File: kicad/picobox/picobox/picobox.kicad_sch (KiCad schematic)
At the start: 31 parts, among them J1 Conn_01x02, J2 Conn_01x03, J3 Conn_01x03, J4 Conn_01x03, J5 Conn_01x03, J6 Conn_01x03, J7 Conn_01x03, J8 Conn_01x03, J9 Conn_01x10, SW1 SW_SPDT, U1 MCP1703Ax-330xxDB

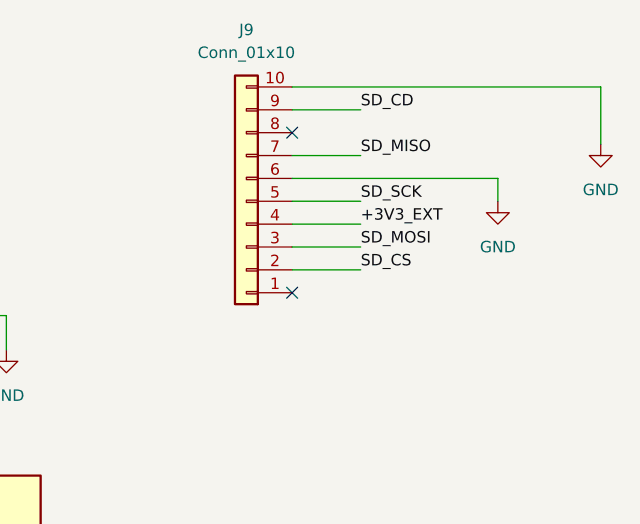
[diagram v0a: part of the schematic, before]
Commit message: feat: PicoBox PCB完成・部品発注完了
- PCBレイアウト・DRC完了（エラー0件）、JLCPCB発注済み（5枚 $4.64）
- J9ピンアサイン修正（SD_CD=PIN10, GND=PIN9）
- Gerberファイル追加（kicad/gerver.zip）
- KiCAD PCBレイアウト・回路図最終版を反映
- docs/pcb_spec.md: 全部品の購入先・品番確定、調達状況セクション追加
  - Mouser: MCP1703 / P6KE6.8CA-TB / SPTAF端子台 / Pico W / SD-15B-05
  - 秋月: 抵抗・コンデンサ・LED・スイッチ・ポリスイッチ 等

Co-Authored-By: Claude Sonnet 4.6 <noreply@anthropic.com>
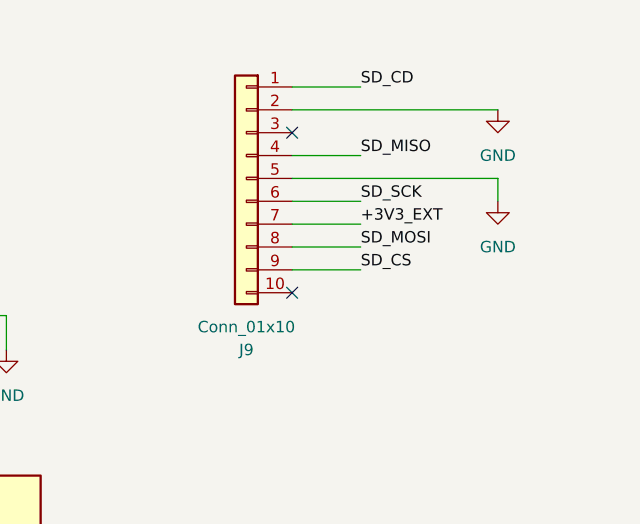
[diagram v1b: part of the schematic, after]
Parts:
- A1: footprint Module:RaspberryPi_Pico_W_SMD_HandSolder -> Module:RaspberryPi_Pico_Common_THT
- C1, C2: footprint (none) -> Capacitor_THT:C_Disc_D5.0mm_W2.5mm_P5.00mm
- C3: footprint (none) -> Capacitor_THT:CP_Radial_D5.0mm_P2.00mm
- C4: footprint (none) -> Capacitor_THT:CP_Radial_D6.3mm_P2.50mm
- D1: footprint (none) -> Diode_THT:D_DO-201AD_P15.24mm_Horizontal
- D2, D3: footprint (none) -> LED_THT:LED_D3.0mm
- F1: footprint (none) -> Varistor:RV_Disc_D9mm_W3.4mm_P5mm
- J1: footprint (none) -> Connector_Phoenix_SPT:PhoenixContact_SPT_1.5_2-H-3.5_1x02_P3.5mm_Horizontal
- J2, J3, J4, J5, J6, J7, J8: footprint (none) -> Connector_JST:JST_PH_B3B-PH-K_1x03_P2.00mm_Vertical
- J9: footprint (none) -> Connector_PinSocket_2.54mm:PinSocket_1x10_P2.54mm_Vertical
- R10, R11, R12, R13, R2, R3, R5, R6, R7, R8, R9: footprint (none) -> Resistor_THT:R_Axial_DIN0207_L6.3mm_D2.5mm_P7.62mm_Horizontal
- SW1: footprint (none) -> Button_Switch_THT:SW_Slide-03_Wuerth-WS-SLTV_10x2.5x6.4_P2.54mm
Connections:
- net +3V3_EXT: now also J9.7 (Pin_7); no longer J9.4 (Pin_4)
- net GND: now also J9.2 (Pin_2), J9.5 (Pin_5); no longer J9.10 (Pin_10), J9.6 (Pin_6)
- net SD_CD: now also J9.1 (Pin_1); no longer J9.9 (Pin_9)
- net SD_CS: now also J9.9 (Pin_9); no longer J9.2 (Pin_2)
- net SD_MISO: now also J9.4 (Pin_4); no longer J9.7 (Pin_7)
- net SD_MOSI: now also J9.8 (Pin_8); no longer J9.3 (Pin_3)
- net SD_SCK: now also J9.6 (Pin_6); no longer J9.5 (Pin_5)
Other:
- moved on the sheet: J9
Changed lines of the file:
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@@
 	(wire
 		(pts
+			(xy 229.87 29.21) (xy 252.73 29.21)
+		)
+		(stroke
+			(width 0)
+			(type default)
+		)
+	)
+	(wire
+		(pts
 			(xy 205.74 116.84) (xy 213.36 116.84)
 		)
@@
 	(wire
 		(pts
-			(xy 264.16 26.67) (xy 264.16 33.02)
-		)
-		(stroke
-			(width 0)
-			(type default)
-		)
-	)
-	(wire
-		(pts
 			(xy 110.49 120.65) (xy 110.49 119.38)
 		)
@@
 	(wire
 		(pts
+			(xy 229.87 26.67) (xy 237.49 26.67)
+		)
+		(stroke
+			(width 0)
+			(type default)
+		)
+	)
+	(wire
+		(pts
 			(xy 111.76 109.22) (xy 111.76 114.3)
 		)
@@
 	(wire
 		(pts
-			(xy 229.87 26.67) (xy 264.16 26.67)
-		)
-		(stroke
-			(width 0)
-			(type default)
-		)
-	)
-	(wire
-		(pts
 			(xy 121.92 60.96) (xy 121.92 41.91)
 		)
@@
 	(wire
 		(pts
-			(xy 229.87 29.21) (xy 237.49 29.21)
-		)
-		(stroke
-			(width 0)
-			(type default)
-		)
-	)
-	(wire
-		(pts
 			(xy 64.77 41.91) (xy 64.77 46.99)
 		)
@@
 	)
 	(label "SD_CD"
-		(at 237.49 29.21 0)
+		(at 237.49 26.67 0)
 		(effects
 			(font
@@
 			)
 		)
-		(property "Footprint" ""
+		(property "Footprint" "Connector_Phoenix_SPT:PhoenixContact_SPT_1.5_2-H-3.5_1x02_P3.5mm_Horizontal"
 			(at 46.99 25.4 0)
 			(effects
@@
 			)
 		)
-		(property "Footprint" ""
+		(property "Footprint" "Resistor_THT:R_Axial_DIN0207_L6.3mm_D2.5mm_P7.62mm_Horizontal"
 			(at 186.182 62.23 90)
 			(effects
@@
 			)
 		)
-		(property "Footprint" ""
+		(property "Footprint" "Connector_JST:JST_PH_B3B-PH-K_1x03_P2.00mm_Vertical"
 			(at 119.38 168.91 0)
 			(effects
@@
 			)
 		)
-		(property "Footprint" ""
+		(property "Footprint" "Resistor_THT:R_Axial_DIN0207_L6.3mm_D2.5mm_P7.62mm_Horizontal"
 			(at 55.372 114.3 90)
 			(effects
@@
 			)
 		)
-		(property "Footprint" ""
+		(property "Footprint" "Diode_THT:D_DO-201AD_P15.24mm_Horizontal"
 			(at 38.1 36.83 0)
 			(effects
@@
 			)
 		)
-		(property "Footprint" ""
+		(property "Footprint" "Resistor_THT:R_Axial_DIN0207_L6.3mm_D2.5mm_P7.62mm_Horizontal"
 			(at 55.372 91.44 90)
 			(effects
@@
 			)
 		)
-		(property "Footprint" ""
+		(property "Footprint" "Capacitor_THT:C_Disc_D5.0mm_W2.5mm_P5.00mm"
 			(at 130.5052 49.53 0)
 			(effects
@@
 			)
 		)
-		(property "Footprint" ""
+		(property "Footprint" "Connector_JST:JST_PH_B3B-PH-K_1x03_P2.00mm_Vertical"
 			(at 68.58 168.91 0)
 			(effects
@@
 	(symbol
 		(lib_id "power:GND")
-		(at 264.16 33.02 0)
+		(at 252.73 29.21 0)
 		(unit 1)
 		(exclude_from_sim no)
@@
 		(fields_autoplaced yes)
 		(property "Reference" "#PWR05"
-			(at 264.16 39.37 0)
+			(at 252.73 35.56 0)
 			(effects
 				(font
@@
 		)
 		(property "Value" "GND"
-			(at 264.16 38.1 0)
+			(at 252.73 34.29 0)
 			(effects
 				(font
@@
 		)
 		(property "Footprint" ""
-			(at 264.16 33.02 0)
+			(at 252.73 29.21 0)
 			(effects
 				(font
@@
 		)
 		(property "Datasheet" ""
-			(at 264.16 33.02 0)
+			(at 252.73 29.21 0)
 			(effects
 				(font
@@
 		)
 		(property "Description" "Power symbol creates a global label with name \"GND\" , ground"
-			(at 264.16 33.02 0)
+			(at 252.73 29.21 0)
 			(effects
 				(font
@@
 			)
 		)
-		(property "Footprint" ""
+		(property "Footprint" "Varistor:RV_Disc_D9mm_W3.4mm_P5mm"
 			(at 48.26 54.61 0)
 			(effects
@@
 			)
 		)
-		(property "Footprint" ""
+		(property "Footprint" "Button_Switch_THT:SW_Slide-03_Wuerth-WS-SLTV_10x2.5x6.4_P2.54mm"
 			(at 57.15 63.5 0)
 			(effects
@@
 			)
 		)
-		(property "Footprint" ""
+		(property "Footprint" "Resistor_THT:R_Axial_DIN0207_L6.3mm_D2.5mm_P7.62mm_Horizontal"
 			(at 102.362 139.7 90)
 			(effects
@@
 			)
 		)
-		(property "Footprint" ""
+		(property "Footprint" "LED_THT:LED_D3.0mm"
 			(at 191.77 52.07 0)
 			(effects
@@
 			)
 		)
-		(property "Footprint" ""
+		(property "Footprint" "Resistor_THT:R_Axial_DIN0207_L6.3mm_D2.5mm_P7.62mm_Horizontal"
 			(at 55.372 139.7 90)
 			(effects
@@
 			)
 		)
-		(property "Footprint" ""
+		(property "Footprint" "Connector_JST:JST_PH_B3B-PH-K_1x03_P2.00mm_Vertical"
 			(at 68.58 95.25 0)
 			(effects
@@
 			)
 		)
-		(property "Footprint" ""
+		(property "Footprint" "Capacitor_THT:C_Disc_D5.0mm_W2.5mm_P5.00mm"
 			(at 154.6352 49.53 0)
 			(effects
@@
 			)
 		)
-		(property "Footprint" "Module:RaspberryPi_Pico_W_SMD_HandSolder"
+		(property "Footprint" "Module:RaspberryPi_Pico_Common_THT"
 			(at 182.88 151.13 0)
 			(effects
@@
 			)
 		)
-		(property "Footprint" ""
+		(property "Footprint" "Resistor_THT:R_Axial_DIN0207_L6.3mm_D2.5mm_P7.62mm_Horizontal"
 			(at 154.432 134.62 90)
 			(effects
@@
 			)
 		)
-		(property "Footprint" ""
+		(property "Footprint" "Resistor_THT:R_Axial_DIN0207_L6.3mm_D2.5mm_P7.62mm_Horizontal"
 			(at 103.632 165.1 90)
 			(effects
@@
 			)
 		)
-		(property "Footprint" ""
+		(property "Footprint" "Capacitor_THT:CP_Radial_D5.0mm_P2.00mm"
 			(at 168.6052 49.53 0)
 			(effects
@@
 			)
 		)
-		(property "Footprint" ""
+		(property "Footprint" "LED_THT:LED_D3.0mm"
 			(at 156.21 142.24 0)
 			(effects
@@
 			)
 		)
-		(property "Footprint" ""
+		(property "Footprint" "Connector_JST:JST_PH_B3B-PH-K_1x03_P2.00mm_Vertical"
 			(at 118.11 143.51 0)
 			(effects
@@
 	(symbol
 		(lib_id "Connector_Generic:Conn_01x10")
-		(at 224.79 39.37 180)
+		(at 224.79 36.83 0)
+		(mirror y)
 		(unit 1)
 		(exclude_from_sim no)
@@
 		(on_board yes)
 		(dnp no)
-		(fields_autoplaced yes)
 		(property "Reference" "J9"
-			(at 224.79 20.32 0)
+			(at 224.79 55.88 0)
 			(effects
 				(font
@@
 		)
 		(property "Value" "Conn_01x10"
-			(at 224.79 22.86 0)
+			(at 224.79 53.34 0)
 			(effects
 				(font
@@
 			)
 		)
-		(property "Footprint" ""
-			(at 224.79 39.37 0)
+		(property "Footprint" "Connector_PinSocket_2.54mm:PinSocket_1x10_P2.54mm_Vertical"
+			(at 224.79 36.83 0)
 			(effects
 				(font
@@
 		)
 		(property "Datasheet" "~"
-			(at 224.79 39.37 0)
+			(at 224.79 36.83 0)
 			(effects
 				(font
@@
 		)
 		(property "Description" "Generic connector, single row, 01x10, script generated (kicad-library-utils/schlib/autogen/connector/)"
-			(at 224.79 39.37 0)
+			(at 224.79 36.83 0)
 			(effects
 				(font
@@
 			)
 		)
-		(property "Footprint" ""
+		(property "Footprint" "Connector_JST:JST_PH_B3B-PH-K_1x03_P2.00mm_Vertical"
 			(at 68.58 143.51 0)
 			(effects
@@
 			)
 		)
-		(property "Footprint" ""
+		(property "Footprint" "Connector_JST:JST_PH_B3B-PH-K_1x03_P2.00mm_Vertical"
 			(at 118.11 116.84 0)
 			(effects
@@
 			)
 		)
-		(property "Footprint" ""
+		(property "Footprint" "Resistor_THT:R_Axial_DIN0207_L6.3mm_D2.5mm_P7.62mm_Horizontal"
 			(at 218.44 113.538 90)
 			(effects
@@
 			)
 		)
-		(property "Footprint" ""
+		(property "Footprint" "Connector_JST:JST_PH_B3B-PH-K_1x03_P2.00mm_Vertical"
 			(at 68.58 118.11 0)
 			(effects
@@
 			)
 		)
-		(property "Footprint" ""
+		(property "Footprint" "Capacitor_THT:CP_Radial_D6.3mm_P2.50mm"
 			(at 105.1052 52.07 0)
 			(effects
@@
 			)
 		)
-		(property "Footprint" ""
+		(property "Footprint" "Resistor_THT:R_Axial_DIN0207_L6.3mm_D2.5mm_P7.62mm_Horizontal"
 			(at 54.102 165.1 90)
 			(effects
@@
 			)
 		)
-		(property "Footprint" ""
+		(property "Footprint" "Resistor_THT:R_Axial_DIN0207_L6.3mm_D2.5mm_P7.62mm_Horizontal"
 			(at 218.44 124.968 90)
 			(effects
@@
 			)
 		)
-		(property "Footprint" ""
+		(property "Footprint" "Resistor_THT:R_Axial_DIN0207_L6.3mm_D2.5mm_P7.62mm_Horizontal"
 			(at 101.092 113.03 90)
 			(effects
